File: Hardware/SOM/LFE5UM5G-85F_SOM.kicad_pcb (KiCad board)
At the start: 6 copper layers, 67.6 x 25.4 mm, 157 parts, among them J1 SODIMM-200_Split, U1 LFE5UM5G-85F, U2 AS4C256M16D3, U3 W25Q128JVP, U4 TPS62A02ADRL, U5 TPS62A02ADRL, U6 TPS62A02ADRL, U7 TPS62A02ADRL

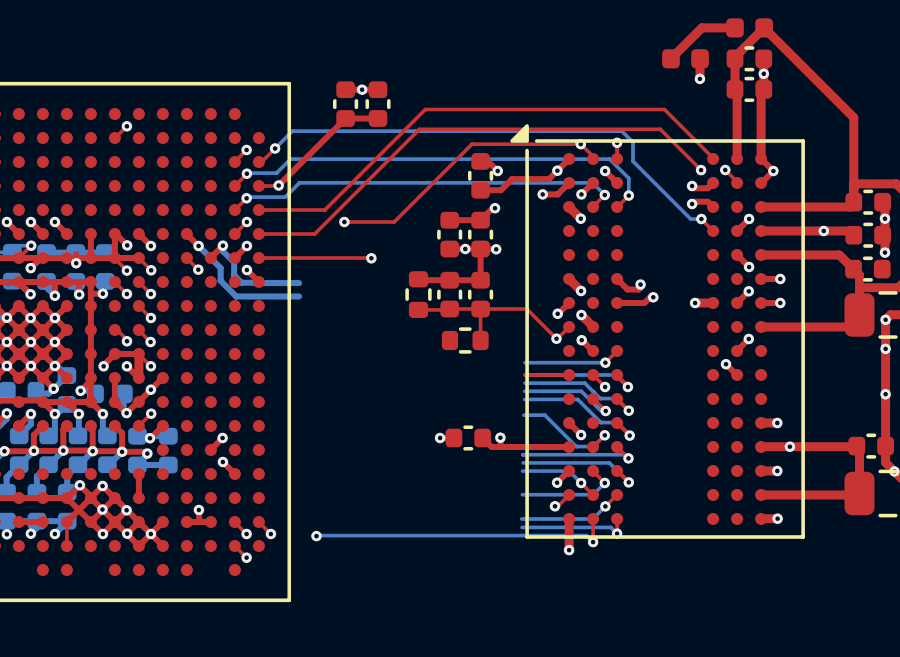
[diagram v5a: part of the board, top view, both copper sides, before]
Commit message: SOM stack-up JLC06161H-3313
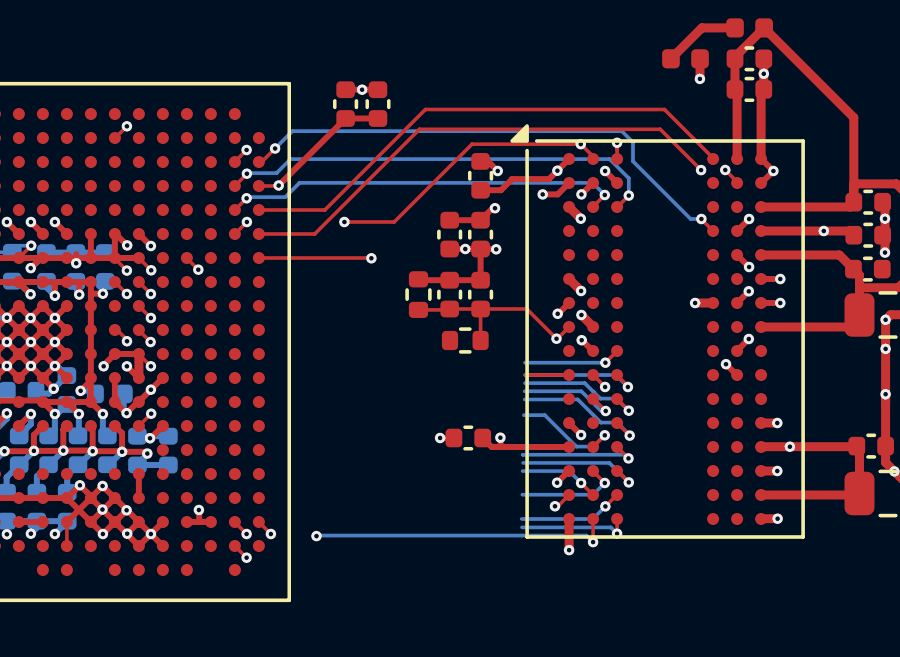
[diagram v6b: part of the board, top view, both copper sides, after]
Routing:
- net DDR_UDQS_P: track 24.3 -> 0.00 mm, vias 2 -> 0
- net DDR_UDQS_N: track 22.8 -> 0.00 mm, vias 2 -> 0
- net DDR_LDQS_N: track 21.5 -> 0.00 mm, vias 2 -> 0
- net DDR_LDQS_P: track 20.2 -> 0.00 mm, vias 2 -> 0
- net DDR_CK_P: track 4.86 -> 0.00 mm, vias 1 -> 0
- net DDR_CK_N: track 3.99 -> 0.00 mm, vias 1 -> 0

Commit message: Switched to 8-layer stack-up JLC08161H-2116
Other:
- copper layers 6 -> 8
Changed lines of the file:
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@@
 	(generator_version "9.0")
 	(general
-		(thickness 1.5584)
+		(thickness 1.6196)
 		(legacy_teardrops no)
 	)
@@
 	(layers
 		(0 "F.Cu" signal)
-		(4 "In1.Cu" power "In1-GND.Cu")
+		(4 "In1.Cu" power "GND-1.Cu")
 		(6 "In2.Cu" signal)
-		(8 "In3.Cu" power "In3-GND.Cu")
-		(10 "In4.Cu" mixed "In4-PWR.Cu")
+		(8 "In3.Cu" power "GND-2.Cu")
+		(10 "In4.Cu" mixed "PWR.Cu")
+		(12 "In5.Cu" signal)
+		(14 "In6.Cu" signal "GND-3.Cu")
 		(2 "B.Cu" signal)
 		(9 "F.Adhes" user "F.Adhesive")
@@
 			(layer "dielectric 1"
 				(type "prepreg")
-				(thickness 0.0994)
+				(thickness 0.1164)
 				(material "FR4")
 				(epsilon_r 4.5)
@@
 			(layer "dielectric 2"
 				(type "core")
-				(thickness 0.55)
+				(thickness 0.3)
 				(material "FR4")
 				(epsilon_r 4.5)
@@
 			(layer "dielectric 3"
 				(type "prepreg")
-				(thickness 0.1088)
+				(thickness 0.0764)
+				(material "FR4")
+				(epsilon_r 4.5)
+				(loss_tangent 0.02) addsublayer
+				(thickness 0.0764)
 				(material "FR4")
 				(epsilon_r 4.5)
@@
 			(layer "dielectric 4"
 				(type "core")
-				(thickness 0.55)
+				(color "FR4 natural")
+				(thickness 0.3)
 				(material "FR4")
 				(epsilon_r 4.5)
@@
 			(layer "dielectric 5"
 				(type "prepreg")
-				(color "#808080FF")
-				(thickness 0.0994)
+				(thickness 0.0764)
 				(material "FR4")
 				(epsilon_r 4.5)
+				(loss_tangent 0.02) addsublayer
+				(thickness 0.0764)
+				(material "FR4")
+				(epsilon_r 4.5)
+				(loss_tangent 0.02)
+			)
+			(layer "In5.Cu"
+				(type "copper")
+				(thickness 0.0152)
+			)
+			(layer "dielectric 6"
+				(type "core")
+				(thickness 0.3)
+				(material "FR4")
+				(epsilon_r 4.5)
+				(loss_tangent 0.02)
+			)
+			(layer "In6.Cu"
+				(type "copper")
+				(thickness 0.0152)
+			)
+			(layer "dielectric 7"
+				(type "prepreg")
+				(thickness 0.1164)
+				(material "FR4")
+				(epsilon_r 4.5)

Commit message: some net names added
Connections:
- C10 pad 2: 3.3V -> 1.5V
- C2 pad 2: 3.3V -> 1.5V
- C6 pad 2: 3.3V -> 1.5V
- U1 pad F10: 3.3V -> 1.5V
- U1 pad F9: 3.3V -> 1.5V
- U1 pad H1: DDR_RAS -> unconnected-(U1F-PL53C-PadH1)
- U1 pad J1: DDR_CS -> unconnected-(U1F-PL53B-PadJ1)
- U1 pad K1: DDR_CAS -> unconnected-(U1F-PL53D-PadK1)
- U1 pad K2: DDR_RST -> unconnected-(U1F-PL53A-PadK2)
- U1 pad K3: DDR_CK -> unconnected-(U1F-PL50D-PadK3)
- U1 pad K4: DDR_WE -> unconnected-(U1F-PL56A-PadK4)
- U1 pad L1: DDR_A12 -> unconnected-(U1F-PL89C-PadL1)
- U1 pad L2: DDR_A9 -> unconnected-(U1F-PL86D-PadL2)
- U1 pad L3: DDR_A8 -> unconnected-(U1F-PL86C-PadL3)
- U1 pad L4: DDR_ODT -> unconnected-(U1F-PL56C-PadL4)
- U1 pad L5: DDR_A0 -> unconnected-(U1F-PL56D-PadL5)
- U1 pad M1: DDR_A11 -> unconnected-(U1F-PL89B-PadM1)
- U1 pad M3: DDR_A7 -> unconnected-(U1F-PL86B-PadM3)
- U1 pad M4: DDR_A2 -> unconnected-(U1F-PL83A-PadM4)
- U1 pad M5: DDR_A1 -> unconnected-(U1F-PL77A-PadM5)
- U1 pad N1: DDR_A13 -> unconnected-(U1F-PL89D-PadN1)
- U1 pad N2: DDR_A10 -> unconnected-(U1F-PL89A-PadN2)
- U1 pad N3: DDR_A6 -> unconnected-(U1F-PL86A-PadN3)
- U1 pad N4: DDR_A4 -> unconnected-(U1F-PL83C-PadN4)
- U1 pad N5: DDR_A3 -> unconnected-(U1F-PL83B-PadN5)
- U1 pad P1: DDR_A14 -> unconnected-(U1F-PL92A-PadP1)
- U1 pad P2: DDR_BA0 -> unconnected-(U1F-PL92B-PadP2)
- U1 pad P3: DDR_BA1 -> unconnected-(U1F-PL92C-PadP3)
- U1 pad P4: DDR_BA2 -> unconnected-(U1F-PL92D-PadP4)
- U1 pad P5: DDR_A5 -> unconnected-(U1F-PL83D-PadP5)
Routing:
- net unconnected-(U1F-PL89A-PadN2): track 0.00 -> 0.58 mm, vias 0 -> 1
- net DDR_A10: track 0.58 -> 0.00 mm, vias 1 -> 0
- net DDR_A5: track 4.05 -> 3.47 mm, vias 2 -> 1
- net unconnected-(U1F-PL83D-PadP5): track 0.00 -> 0.58 mm, vias 0 -> 1
- net unconnected-(U1F-PL83B-PadN5): track 0.00 -> 0.58 mm, vias 0 -> 1
- net DDR_A3: track 4.42 -> 3.84 mm, vias 2 -> 1
- net DDR_BA2: track 5.18 -> 4.61 mm, vias 2 -> 1
- net unconnected-(U1F-PL92D-PadP4): track 0.00 -> 0.57 mm, vias 0 -> 1
- net unconnected-(U1F-PL92B-PadP2): track 0.00 -> 0.57 mm, vias 0 -> 1
- net DDR_BA0: track 0.57 -> 0.00 mm, vias 1 -> 0
- net unconnected-(U1F-PL92C-PadP3): track 0.00 -> 0.57 mm, vias 0 -> 1
- net DDR_BA1: track 0.57 -> 0.00 mm, vias 1 -> 0
- net DDR_WE: track 4.96 -> 4.39 mm, vias 2 -> 1
- net unconnected-(U1F-PL56A-PadK4): track 0.00 -> 0.57 mm, vias 0 -> 1
- net unconnected-(U1F-PL50D-PadK3): track 0.00 -> 0.57 mm, vias 0 -> 1
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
